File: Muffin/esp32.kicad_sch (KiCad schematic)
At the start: 19 parts, among them J10 I2C_STEMMA, J11 TRAINER, J12 Gimbal, J15 EXTMOD, J17 Micro_SD_Card, J18 INTMOD, J19 TouchPanel, J20 LCD, Q2 AO3400A, U4 ESP32-S3-WROOM-1U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

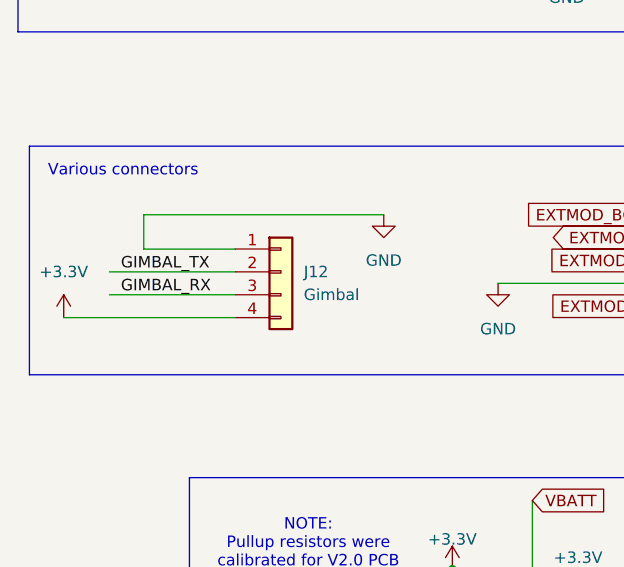
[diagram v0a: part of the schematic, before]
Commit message: PCB 2.1
Fixed a reversed ZH-socket on the board for Gimbal
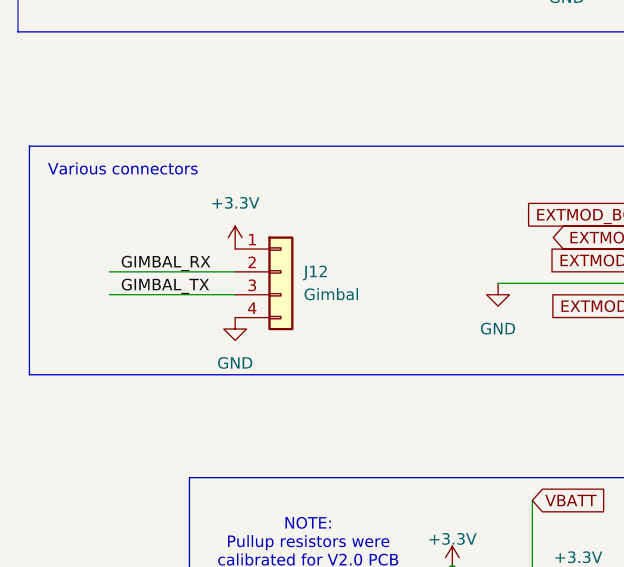
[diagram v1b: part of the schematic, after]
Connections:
- net +3.3V: now also J12.1 (Pin_1); no longer J12.4 (Pin_4)
- net GIMBAL_RX: now also J12.2 (Pin_2); no longer J12.3 (Pin_3)
- net GIMBAL_TX: now also J12.3 (Pin_3); no longer J12.2 (Pin_2)
- net GND: now also J12.4 (Pin_4); no longer J12.1 (Pin_1)
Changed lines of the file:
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@@
 	(wire
 		(pts
-			(xy 30.48 120.65) (xy 30.48 124.46)
-		)
-		(stroke
-			(width 0)
-			(type default)
-		)
-	)
-	(wire
-		(pts
 			(xy 204.47 74.93) (xy 204.47 82.55)
 		)
@@
 	(wire
 		(pts
-			(xy 57.15 120.65) (xy 30.48 120.65)
-		)
-		(stroke
-			(width 0)
-			(type default)
-		)
-	)
-	(wire
-		(pts
 			(xy 124.46 180.34) (xy 124.46 179.07)
 		)
@@
 	(wire
 		(pts
-			(xy 30.48 124.46) (xy 40.64 124.46)
-		)
-		(stroke
-			(width 0)
-			(type default)
-		)
-	)
-	(wire
-		(pts
 			(xy 88.9 123.19) (xy 95.25 123.19)
 		)
@@
 	(wire
 		(pts
-			(xy 21.59 132.08) (xy 40.64 132.08)
-		)
-		(stroke
-			(width 0)
-			(type default)
-		)
-	)
-	(wire
-		(pts
 			(xy 48.26 66.04) (xy 62.23 66.04)
 		)
@@
 		)
 	)
-	(label "GIMBAL_RX"
-		(at 27.94 129.54 0)
-		(fields_autoplaced yes)
-		(effects
-			(font
-				(size 1.27 1.27)
-			)
-			(justify left bottom)
-		)
-	)
 	(label "LCD_RS"
 		(at 250.19 43.18 0)
@@
 		)
 	)
-	(label "GIMBAL_TX"
-		(at 27.94 127 0)
+	(label "LCD_D2"
+		(at 49.53 76.2 0)
 		(fields_autoplaced yes)
 		(effects
@@
 		)
 	)
-	(label "LCD_D2"
-		(at 49.53 76.2 0)
+	(label "LCD_D3"
+		(at 250.19 68.58 0)
 		(fields_autoplaced yes)
 		(effects
@@
 		)
 	)
-	(label "LCD_D3"
-		(at 250.19 68.58 0)
+	(label "GIMBAL_RX"
+		(at 27.94 127 0)
 		(fields_autoplaced yes)
 		(effects
@@
 		)
 	)
+	(label "GIMBAL_TX"
+		(at 27.94 129.54 0)
+		(fields_autoplaced yes)
+		(effects
+			(font
+				(size 1.27 1.27)
+			)
+			(justify left bottom)
+		)
+	)
 	(label "TOUCH_INT"
 		(at 195.58 69.85 0)
@@
 	(symbol
 		(lib_id "power:GND")
-		(at 57.15 120.65 0)
+		(at 40.64 132.08 0)
 		(unit 1)
 		(exclude_from_sim no)
@@
 		(fields_autoplaced yes)
 		(property "Reference" "#PWR045"
-			(at 57.15 127 0)
+			(at 40.64 138.43 0)
 			(effects
 				(font
@@
 		)
 		(property "Value" "GND"
-			(at 57.15 125.73 0)
+			(at 40.64 137.16 0)
 			(effects
 				(font
@@
 		)
 		(property "Footprint" ""
-			(at 57.15 120.65 0)
+			(at 40.64 132.08 0)
 			(effects
 				(font
@@
 		)
 		(property "Datasheet" ""
-			(at 57.15 120.65 0)
+			(at 40.64 132.08 0)
 			(effects
 				(font
@@
 		)
 		(property "Description" "Power symbol creates a global label with name \"GND\" , ground"
-			(at 57.15 120.65 0)
+			(at 40.64 132.08 0)
 			(effects
 				(font
@@
 	(symbol
 		(lib_id "power:+3.3V")
-		(at 21.59 132.08 0)
+		(at 40.64 124.46 0)
 		(unit 1)
 		(exclude_from_sim no)
@@
 		(fields_autoplaced yes)
 		(property "Reference" "#PWR044"
-			(at 21.59 135.89 0)
+			(at 40.64 128.27 0)
 			(effects
 				(font
@@
 		)
 		(property "Value" "+3.3V"
-			(at 21.59 127 0)
+			(at 40.64 119.38 0)
 			(effects
 				(font
@@
 		)
 		(property "Footprint" ""
-			(at 21.59 132.08 0)
+			(at 40.64 124.46 0)
 			(effects
 				(font
@@
 		)
 		(property "Datasheet" ""
-			(at 21.59 132.08 0)
+			(at 40.64 124.46 0)
 			(effects
 				(font
@@
 		)
 		(property "Description" "Power symbol creates a global label with name \"+3.3V\""
-			(at 21.59 132.08 0)
+			(at 40.64 124.46 0)
 			(effects
 				(font
